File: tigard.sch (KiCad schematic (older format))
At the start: 52 parts, among them J1 USB_C_Receptacle_USB2.0, J2 JTAG, J3 UART, J4 SPI, J5 SWD, J6 I2C, Q1 BSH103, SW1 SW_SP3T, SW2 SW_DPDT, U1 AP7365-18, U2 AP7365-33, U3 FT2232HQ, U4 93LCxxBxxOT, Y1 12MHz

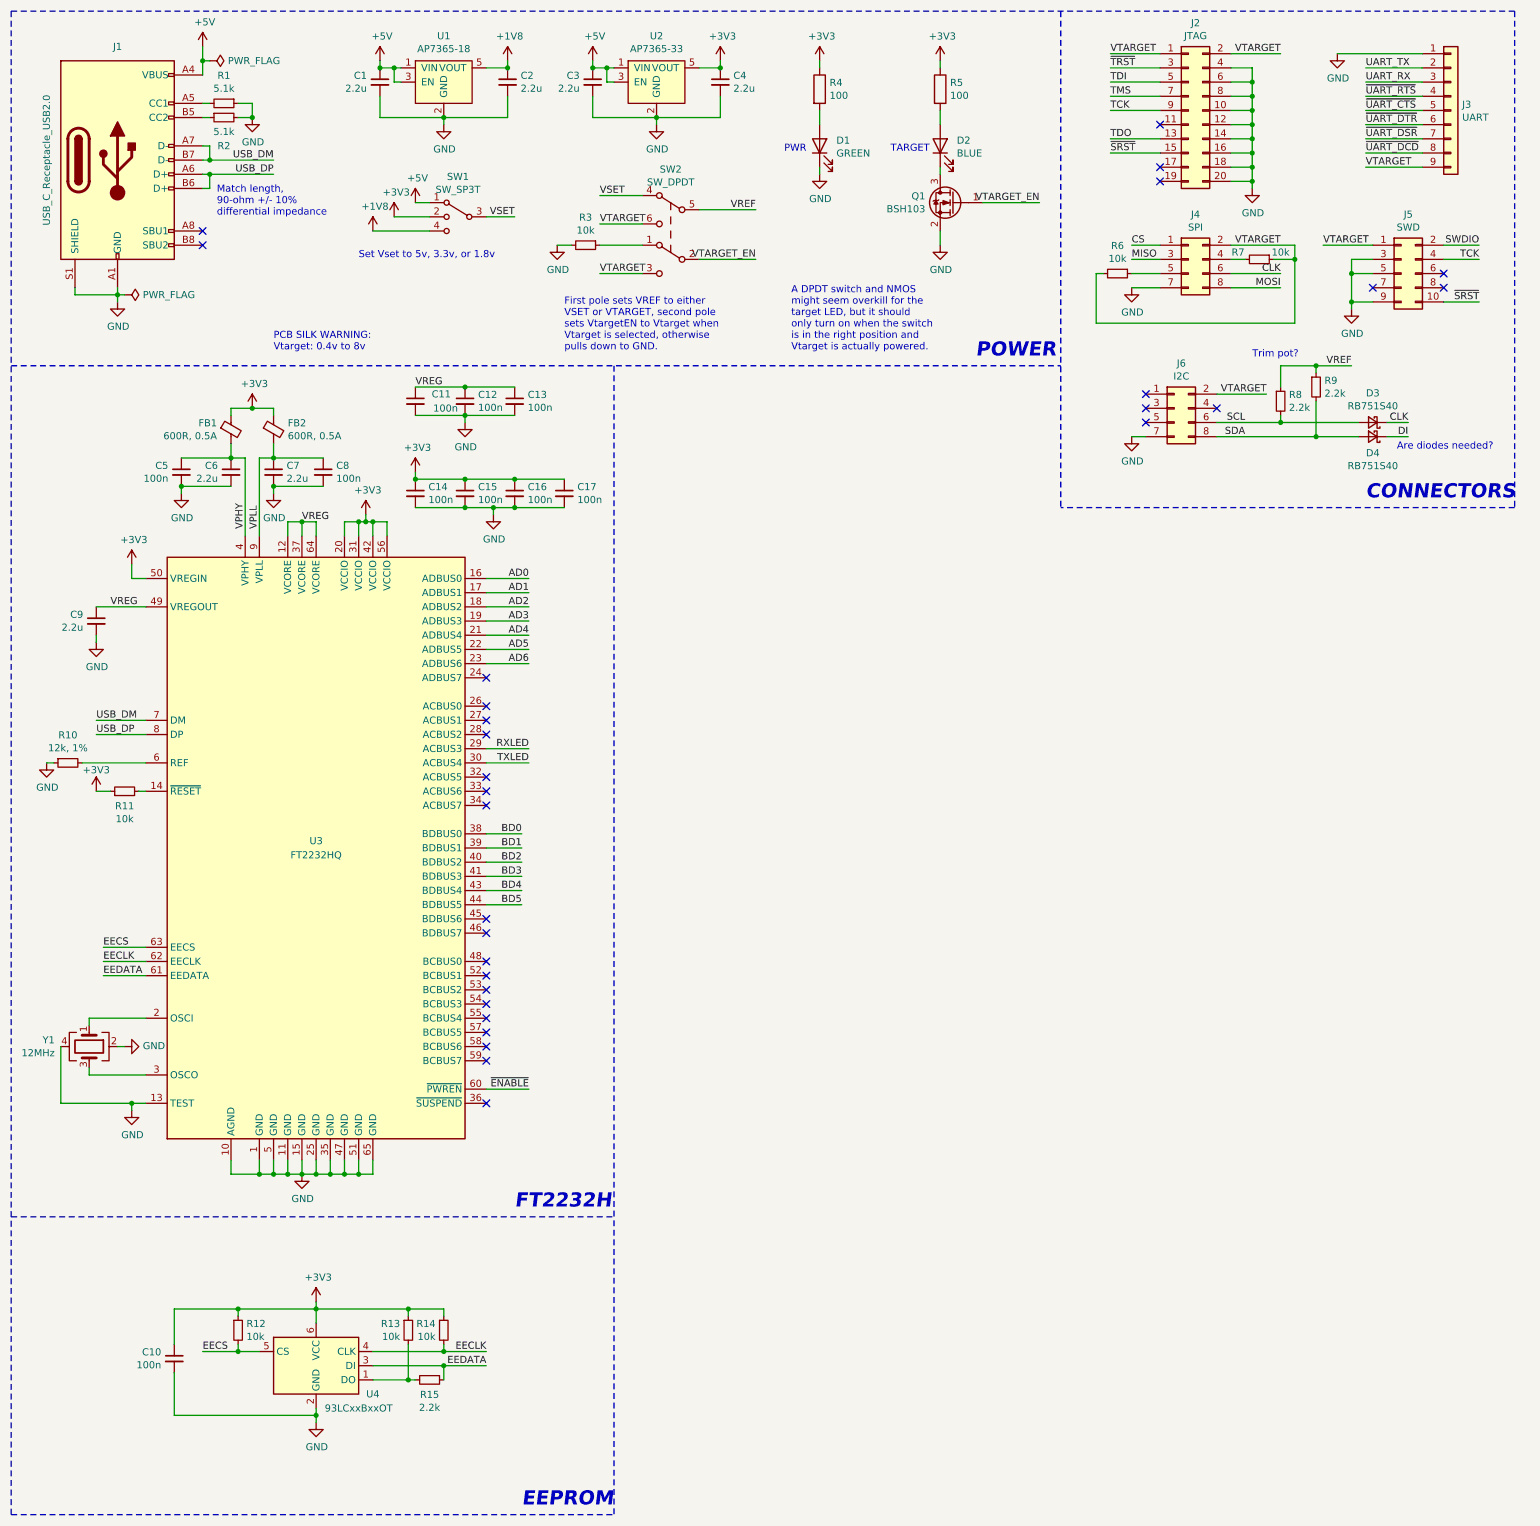
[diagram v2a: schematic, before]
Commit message: Initial work for input/output buffers
* Still need to decide on a footprint for them
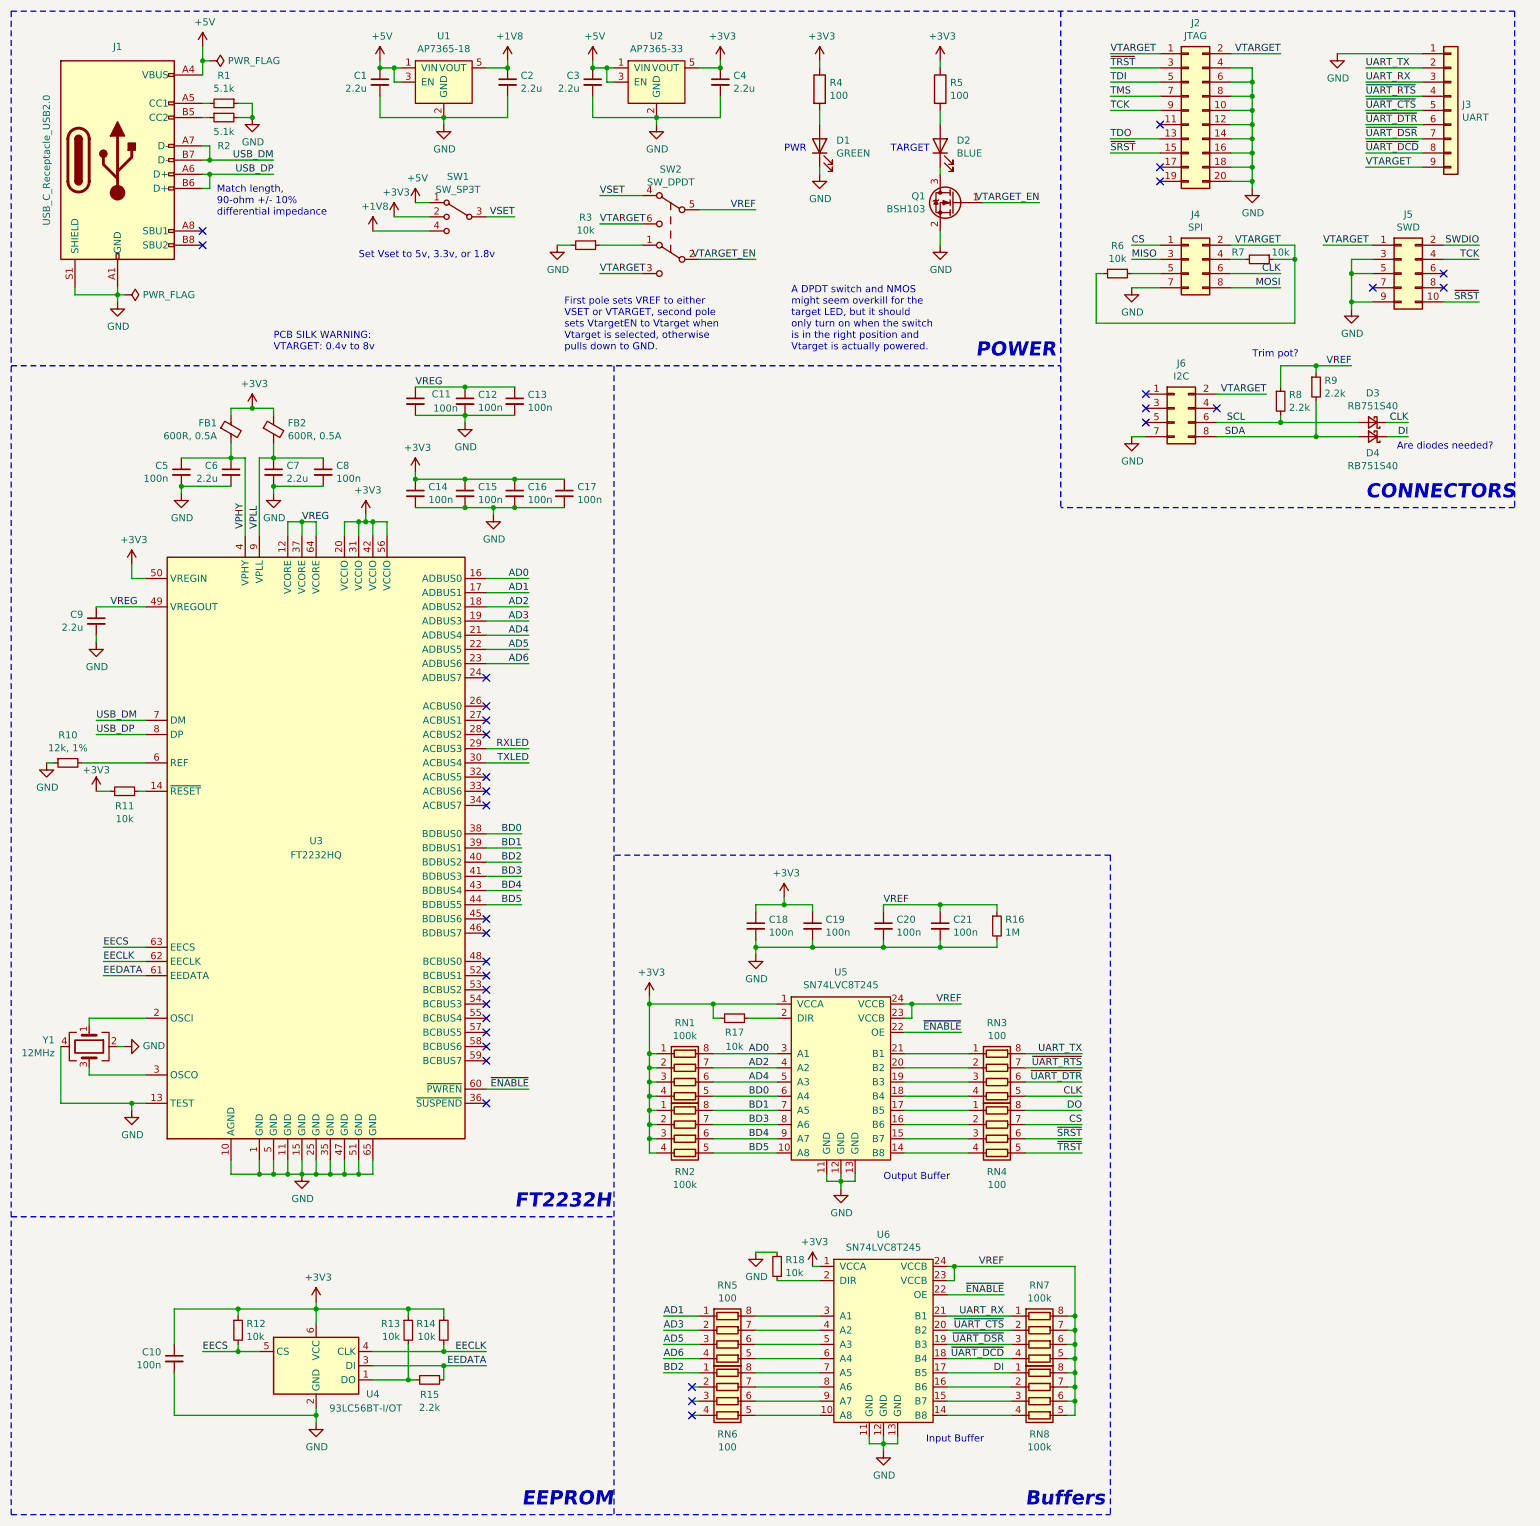
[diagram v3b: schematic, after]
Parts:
- added C18, C19, C20, C21: 100n, Capacitor_SMD:C_0402_1005Metric, symbol Device:C_Small
- added R16: 1M, Resistor_SMD:R_0402_1005Metric, symbol Device:R_Small
- added R17, R18: 10k, Resistor_SMD:R_0402_1005Metric, symbol Device:R_Small
- added RN1, RN2, RN7, RN8: 100k, Resistor_SMD:R_Array_Convex_4x0402, symbol Device:R_Pack04
- added RN3, RN4, RN5, RN6: 100, Resistor_SMD:R_Array_Convex_4x0402, symbol Device:R_Pack04
- added U5, U6: SN74LVC8T245, symbol tigard:SN74LVC8T245
- U4: value 93LCxxBxxOT -> 93LC56BT-I/OT; LCSC (none) -> C190271; P/N (none) -> 93LC56BT-I/OT
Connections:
- net +3V3: now also C18.1, C19.1, R17.1, RN1.1 (R1.1), RN1.2 (R2.1), RN1.3 (R3.1), RN1.4 (R4.1), RN2.1 (R1.1), RN2.2 (R2.1), RN2.3 (R3.1), RN2.4 (R4.1), U5.1 (VCCA), U6.1 (VCCA)
- net AD0: now also RN1.8 (R1.2), U5.3 (A1)
- net AD1: now also RN5.1 (R1.1)
- net AD2: now also RN1.7 (R2.2), U5.4 (A2)
- net AD3: now also RN5.2 (R2.1)
- net AD4: now also RN1.6 (R3.2), U5.5 (A3)
- net AD5: now also RN5.3 (R3.1)
- net AD6: now also RN5.4 (R4.1)
- net BD0: now also RN1.5 (R4.2), U5.6 (A4)
- net BD1: now also RN2.8 (R1.2), U5.7 (A5)
- net BD2: now also RN6.1 (R1.1)
- net BD3: now also RN2.7 (R2.2), U5.8 (A6)
- net BD4: now also RN2.6 (R3.2), U5.9 (A7)
- net BD5: now also RN2.5 (R4.2), U5.10 (A8)
- net CLK: now also RN3.5 (R4.2)
- net CS: now also RN4.7 (R2.2)
- net DI: now also RN8.1 (R1.1), U6.17 (B5)
- net GND: now also C18.2, C19.2, C20.2, C21.2, R16.2, R18.2, U5.11 (GND), U5.12 (GND), U5.13 (GND), U6.11 (GND), U6.12 (GND), U6.13 (GND)
- net UART_RX: now also RN7.1 (R1.1), U6.21 (B1)
- net UART_TX: now also RN3.8 (R1.2)
- net VREF: now also C20.1, C21.1, R16.1, RN7.5 (R4.2), RN7.6 (R3.2), RN7.7 (R2.2), RN7.8 (R1.2), RN8.5 (R4.2), RN8.6 (R3.2), RN8.7 (R2.2), RN8.8 (R1.2), U5.23 (VCCB), U5.24 (VCCB), U6.23 (VCCB), U6.24 (VCCB)
- net ~ENABLE: now also U5.22 (OE), U6.22 (OE)
- net ~SRST: now also RN4.6 (R3.2)
- net ~TRST: now also RN4.5 (R4.2)
- net ~UART_CTS: now also RN7.2 (R2.1), U6.20 (B2)
- net ~UART_DCD: now also RN7.4 (R4.1), U6.18 (B4)
- net ~UART_DSR: now also RN7.3 (R3.1), U6.19 (B3)
- net ~UART_DTR: now also RN3.6 (R3.2)
- net ~UART_RTS: now also RN3.7 (R2.2)
- new net: RN4.4 (R4.1), U5.14 (B8)
- new net: RN4.3 (R3.1), U5.15 (B7)
- new net: RN4.2 (R2.1), U5.16 (B6)
- new net: RN4.1 (R1.1), U5.17 (B5)
- new net: RN3.4 (R4.1), U5.18 (B4)
- new net: RN3.3 (R3.1), U5.19 (B3)
- new net: R17.2, U5.2 (DIR)
- new net: RN3.2 (R2.1), U5.20 (B2)
- new net: RN3.1 (R1.1), U5.21 (B1)
- new net: RN6.5 (R4.2), U6.10 (A8)
- new net: RN8.4 (R4.1), U6.14 (B8)
- new net: RN8.3 (R3.1), U6.15 (B7)
- new net: RN8.2 (R2.1), U6.16 (B6)
- new net: R18.1, U6.2 (DIR)
- new net: RN5.8 (R1.2), U6.3 (A1)
- new net: RN5.7 (R2.2), U6.4 (A2)
- new net: RN5.6 (R3.2), U6.5 (A3)
- new net: RN5.5 (R4.2), U6.6 (A4)
- new net: RN6.8 (R1.2), U6.7 (A5)
- new net: RN6.7 (R2.2), U6.8 (A6)
- new net: RN6.6 (R3.2), U6.9 (A7)
- new net DO: RN4.8 (R1.2)
- no-connect marks 30 -> 33
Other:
- note added: "Buffers"
- note added: "Input Buffer"
- note added: "Output Buffer"
- note added: "PCB SILK WARNING:\nVTARGET: 0.4v to 8v"
- note removed: "PCB SILK WARNING:\nVtarget: 0.4v to 8v"

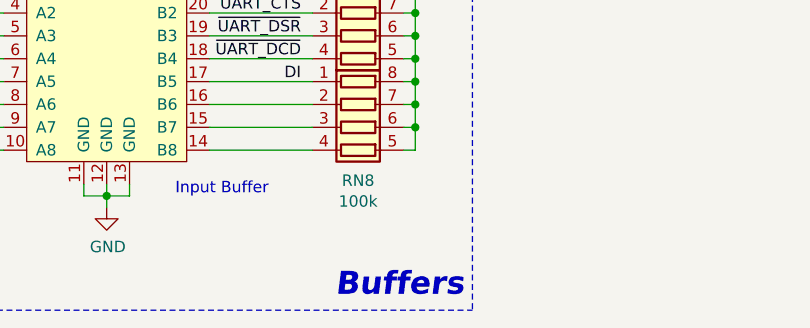
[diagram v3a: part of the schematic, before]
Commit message: Add RHL-24 footprint for buffers
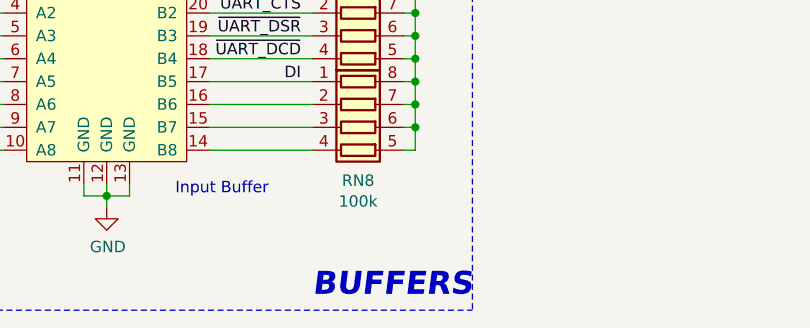
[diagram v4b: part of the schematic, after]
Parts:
- U5, U6: footprint (none) -> tigard:Texas_VQFN-RHL-24_ThermalVias; LCSC (none) -> C350563; P/N (none) -> SN74LVC8T245RHLR
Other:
- note added: "BUFFERS"
- note removed: "Buffers"
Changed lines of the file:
@@
 F 0 "U5" H 6400 9075 50  0000 C CNN
 F 1 "SN74LVC8T245" H 6400 8984 50  0000 C CNN
-F 2 "" H 6400 8300 50  0001 C CNN
+F 2 "tigard:Texas_VQFN-RHL-24_ThermalVias" H 6400 8300 50  0001 C CNN
 F 3 "" H 6400 8300 50  0001 C CNN
+F 4 "SN74LVC8T245RHLR" H 6400 8200 50  0001 C CNN "P/N"
+F 5 "C350563" H 6400 8200 50  0001 C CNN "LCSC"
 	1    6400 8200
 	1    0    0    -1
@@
 F 0 "U6" H 6700 10925 50  0000 C CNN
 F 1 "SN74LVC8T245" H 6700 10834 50  0000 C CNN
-F 2 "" H 6700 10150 50  0001 C CNN
+F 2 "tigard:Texas_VQFN-RHL-24_ThermalVias" H 6700 10150 50  0001 C CNN
 F 3 "" H 6700 10150 50  0001 C CNN
+F 4 "SN74LVC8T245RHLR" H 6700 10050 50  0001 C CNN "P/N"
+F 5 "C350563" H 6700 10050 50  0001 C CNN "LCSC"
 	1    6700 10050
 	1    0    0    -1
@@
 Wire Wire Line
 	5150 9750 5400 9750
-Text Notes 7700 11100 0    100  Italic 20
-Buffers
+Text Notes 7600 11100 0    100  Italic 20
+BUFFERS
 Wire Notes Line
 	550  11150 8300 11150
